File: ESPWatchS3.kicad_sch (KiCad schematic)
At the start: 109 parts, among them J1 OLED, J2 USB, J3 UART0, U1 ESP32-S3R8, U10 BD48KxxG, U2 EVA-M8Q-0, U3 BME280, U4 IS25LP128F-JKLE, U5 BQ27441-G1A, U6 BQ24075RGTR, U7 TPS631000DRLR, U8 AP3012, U9 NJG1143UA2-TE1, Y1 40MHz, Y2 32.768kHz, Y3 32.768kHz

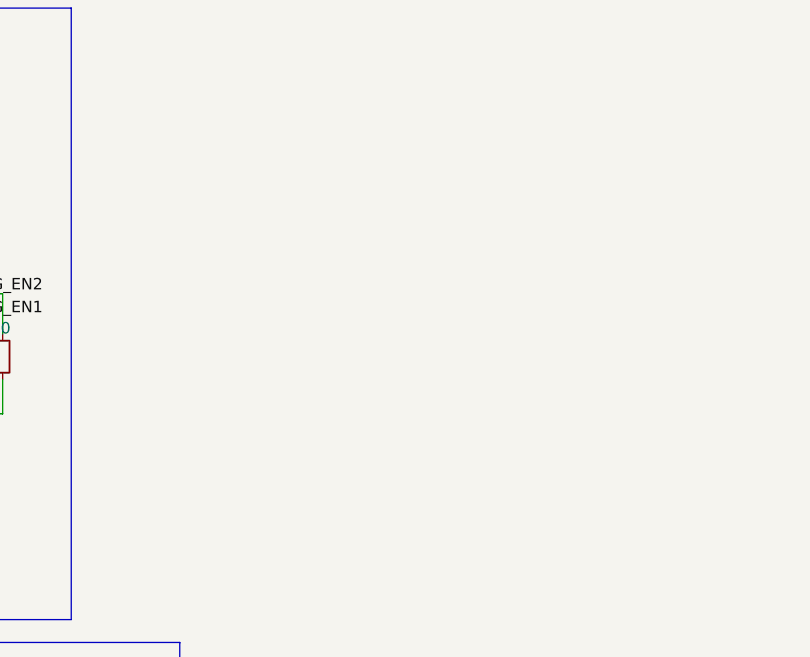
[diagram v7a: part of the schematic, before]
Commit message: Update schematic to add mounting holes
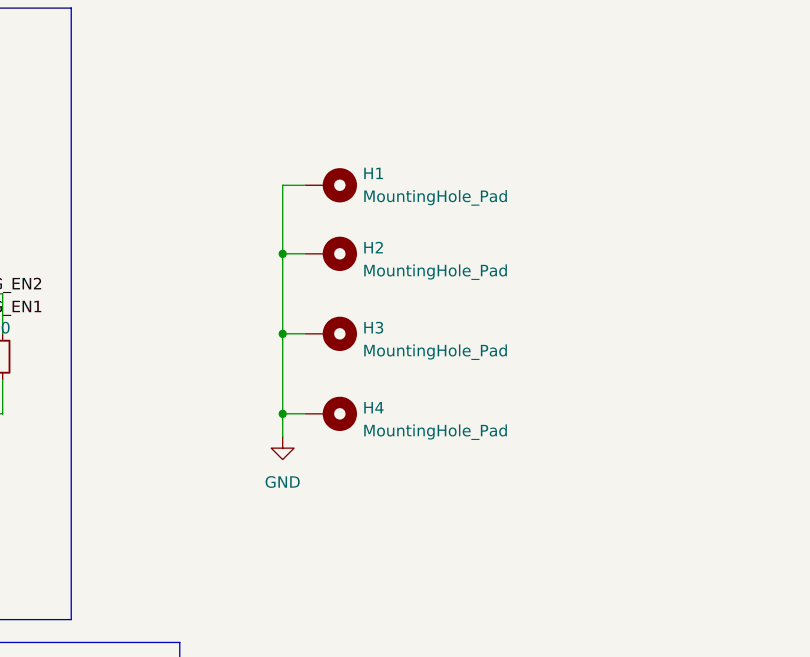
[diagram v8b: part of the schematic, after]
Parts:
- added H1, H2, H3, H4: MountingHole_Pad, MountingHole:MountingHole_2.2mm_M2_Pad, symbol Mechanical:MountingHole_Pad
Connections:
- net EP: now also H1.1, H2.1, H3.1, H4.1
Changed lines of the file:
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@@
   (junction (at 155.575 32.385) (diameter 0) (color 0 0 0 0)
   )
+  (junction (at 177.8 195.58) (diameter 0) (color 0 0 0 0)
+  )
   (junction (at 142.875 187.325) (diameter 0) (color 0 0 0 0)
   )
@@
   (junction (at 132.715 34.925) (diameter 0) (color 0 0 0 0)
   )
+  (junction (at 177.8 213.36) (diameter 0) (color 0 0 0 0)
+  )
   (junction (at 47.625 67.945) (diameter 0) (color 0 0 0 0)
   )
@@
   (junction (at 51.435 67.945) (diameter 0) (color 0 0 0 0)
   )
+  (junction (at 177.8 204.47) (diameter 0) (color 0 0 0 0)
+  )
   (junction (at 278.765 73.66) (diameter 0) (color 0 0 0 0)
   )
@@
   (no_connect (at 132.715 93.345))
   (no_connect (at 132.715 98.425))
+  (wire (pts (xy 177.8 187.96) (xy 180.34 187.96))
+    (stroke (width 0) (type default))
+  )
   (wire (pts (xy 117.475 182.245) (xy 118.745 182.245))
     (stroke (width 0) (type default))
@@
     (stroke (width 0) (type default))
   )
+  (wire (pts (xy 177.8 195.58) (xy 180.34 195.58))
+    (stroke (width 0) (type default))
+  )
   (wire (pts (xy 213.995 43.18) (xy 213.995 45.72))
     (stroke (width 0) (type default))
@@
     (stroke (width 0) (type default))
   )
+  (wire (pts (xy 177.8 195.58) (xy 177.8 187.96))
+    (stroke (width 0) (type default))
+  )
   (wire (pts (xy 278.765 130.81) (xy 278.765 133.35))
     (stroke (width 0) (type default))
@@
     (stroke (width 0) (type default))
   )
+  (wire (pts (xy 177.8 213.36) (xy 177.8 215.9))
+    (stroke (width 0) (type default))
+  )
   (wire (pts (xy 106.045 184.785) (xy 106.045 187.325))
     (stroke (width 0) (type default))
@@
     (stroke (width 0) (type default))
   )
+  (wire (pts (xy 177.8 213.36) (xy 177.8 204.47))
+    (stroke (width 0) (type default))
+  )
   (wire (pts (xy 227.965 142.875) (xy 227.965 145.415))
     (stroke (width 0) (type default))
@@
     (stroke (width 0) (type default))
   )
+  (wire (pts (xy 177.8 204.47) (xy 177.8 195.58))
+    (stroke (width 0) (type default))
+  )
   (wire (pts (xy 51.435 55.245) (xy 81.915 55.245))
     (stroke (width 0) (type default))
@@
     (stroke (width 0) (type default))
   )
+  (wire (pts (xy 177.8 204.47) (xy 180.34 204.47))
+    (stroke (width 0) (type default))
+  )
   (wire (pts (xy 344.805 100.33) (xy 344.805 104.14))
     (stroke (width 0) (type default))
@@
     (stroke (width 0) (type default))
   )
+  (wire (pts (xy 180.34 213.36) (xy 177.8 213.36))
+    (stroke (width 0) (type default))
+  )
   (wire (pts (xy 73.66 267.97) (xy 73.66 270.51))
     (stroke (width 0) (type default))
@@
     )
   )
+  (symbol (lib_id "Mechanical:MountingHole_Pad") (at 182.88 204.47 270) (unit 1)
+    (in_bom yes) (on_board yes) (dnp no) (fields_autoplaced)
+    (property "Reference" "H3" (at 186.69 203.835 90)
+      (effects (font (size 1.27 1.27)) (justify left))
+    )
+    (property "Value" "MountingHole_Pad" (at 186.69 206.375 90)
+      (effects (font (size 1.27 1.27)) (justify left))
+    )
+    (property "Footprint" "MountingHole:MountingHole_2.2mm_M2_Pad" (at 182.88 204.47 0)
+      (effects (font (size 1.27 1.27)) hide)
+    )
+    (property "Datasheet" "~" (at 182.88 204.47 0)
+      (effects (font (size 1.27 1.27)) hide)
+    )
+    (pin "1")
+    (instances
+      (project "ESPWatchS3"
+        (path "/bf5b2c41-bb33-4360-ba29-22d569e03292"
+          (reference "H3") (unit 1)
+        )
+      )
+    )
+  )
   (symbol (lib_id "power:+3V3") (at 61.595 147.955 0) (unit 1)
     (in_bom yes) (on_board yes) (dnp no) (fields_autoplaced)
@@
     )
   )
+  (symbol (lib_id "Mechanical:MountingHole_Pad") (at 182.88 187.96 270) (unit 1)
+    (in_bom yes) (on_board yes) (dnp no)
+    (property "Reference" "H1" (at 186.69 186.69 90)
+      (effects (font (size 1.27 1.27)) (justify left))
+    )
+    (property "Value" "MountingHole_Pad" (at 186.69 189.23 90)
+      (effects (font (size 1.27 1.27)) (justify left))
+    )
+    (property "Footprint" "MountingHole:MountingHole_2.2mm_M2_Pad" (at 182.88 187.96 0)
+      (effects (font (size 1.27 1.27)) hide)
+    )
+    (property "Datasheet" "~" (at 182.88 187.96 0)
+      (effects (font (size 1.27 1.27)) hide)
+    )
+    (pin "1")
+    (instances
+      (project "ESPWatchS3"
+        (path "/bf5b2c41-bb33-4360-ba29-22d569e03292"
+          (reference "H1") (unit 1)
+        )
+      )
+    )
+  )
   (symbol (lib_id "power:GND") (at 25.4 267.97 0) (unit 1)
     (in_bom yes) (on_board yes) (dnp no) (fields_autoplaced)
@@
     )
   )
+  (symbol (lib_id "Mechanical:MountingHole_Pad") (at 182.88 213.36 270) (unit 1)
+    (in_bom yes) (on_board yes) (dnp no) (fields_autoplaced)
+    (property "Reference" "H4" (at 186.69 212.725 90)
+      (effects (font (size 1.27 1.27)) (justify left))
+    )
+    (property "Value" "MountingHole_Pad" (at 186.69 215.265 90)
+      (effects (font (size 1.27 1.27)) (justify left))
+    )
+    (property "Footprint" "MountingHole:MountingHole_2.2mm_M2_Pad" (at 182.88 213.36 0)
+      (effects (font (size 1.27 1.27)) hide)
+    )
+    (property "Datasheet" "~" (at 182.88 213.36 0)
+      (effects (font (size 1.27 1.27)) hide)
+    )
+    (pin "1")
+    (instances
+      (project "ESPWatchS3"
+        (path "/bf5b2c41-bb33-4360-ba29-22d569e03292"
+          (reference "H4") (unit 1)
+        )
+      )
+    )
+  )
   (symbol (lib_id "Device:R_Small") (at 182.245 64.135 180) (unit 1)
     (in_bom yes) (on_board yes) (dnp no)
@@
     )
   )
+  (symbol (lib_id "power:GND") (at 177.8 215.9 0) (unit 1)
+    (in_bom yes) (on_board yes) (dnp no) (fields_autoplaced)
+    (property "Reference" "#PWR013" (at 177.8 222.25 0)
+      (effects (font (size 1.27 1.27)) hide)
+    )
+    (property "Value" "GND" (at 177.8 220.98 0)
+      (effects (font (size 1.27 1.27)))
+    )
+    (property "Footprint" "" (at 177.8 215.9 0)
+      (effects (font (size 1.27 1.27)) hide)
+    )
+    (property "Datasheet" "" (at 177.8 215.9 0)
+      (effects (font (size 1.27 1.27)) hide)
+    )
+    (pin "1")
+    (instances
+      (project "ESPWatchS3"
+        (path "/bf5b2c41-bb33-4360-ba29-22d569e03292"
+          (reference "#PWR013") (unit 1)
+        )
+      )
+    )
+  )
   (symbol (lib_id "Device:R_Small") (at 137.16 38.735 180) (unit 1)
     (in_bom yes) (on_board yes) (dnp no)
@@
         )
       )
+    )
+  )
+  (symbol (lib_id "Mechanical:MountingHole_Pad") (at 182.88 195.58 270) (unit 1)
+    (in_bom yes) (on_board yes) (dnp no) (fields_autoplaced)
+    (property "Reference" "H2" (at 186.69 194.945 90)
+      (effects (font (size 1.27 1.27)) (justify left))
+    )
+    (property "Value" "MountingHole_Pad" (at 186.69 197.485 90)
+      (effects (font (size 1.27 1.27)) (justify left))
+    )
+    (property "Footprint" "MountingHole:MountingHole_2.2mm_M2_Pad" (at 182.88 195.58 0)
+      (effects (font (size 1.27 1.27)) hide)
+    )
+    (property "Datasheet" "~" (at 182.88 195.58 0)
+      (effects (font (size 1.27 1.27)) hide)
+    )
+    (pin "1")
+    (instances
+      (project "ESPWatchS3"
+        (path "/bf5b2c41-bb33-4360-ba29-22d569e03292"
+          (reference "H2") (unit 1)
+        )
+      )
